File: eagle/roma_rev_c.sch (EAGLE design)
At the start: 23 parts, among them IC1 78L12, U1 LTC3426

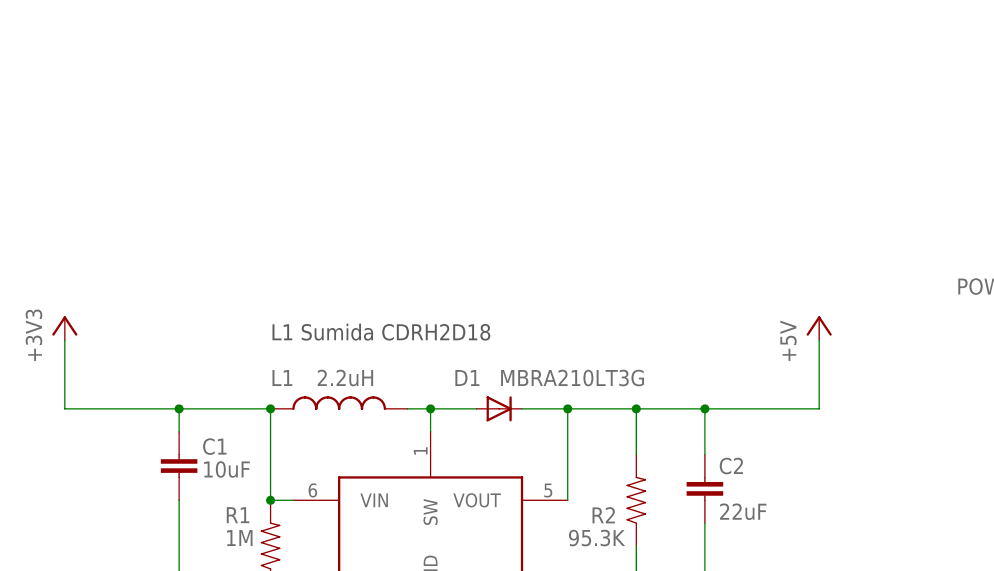
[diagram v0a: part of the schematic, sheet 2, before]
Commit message: Added solder short to get +5V from Odessa 5V without converter.
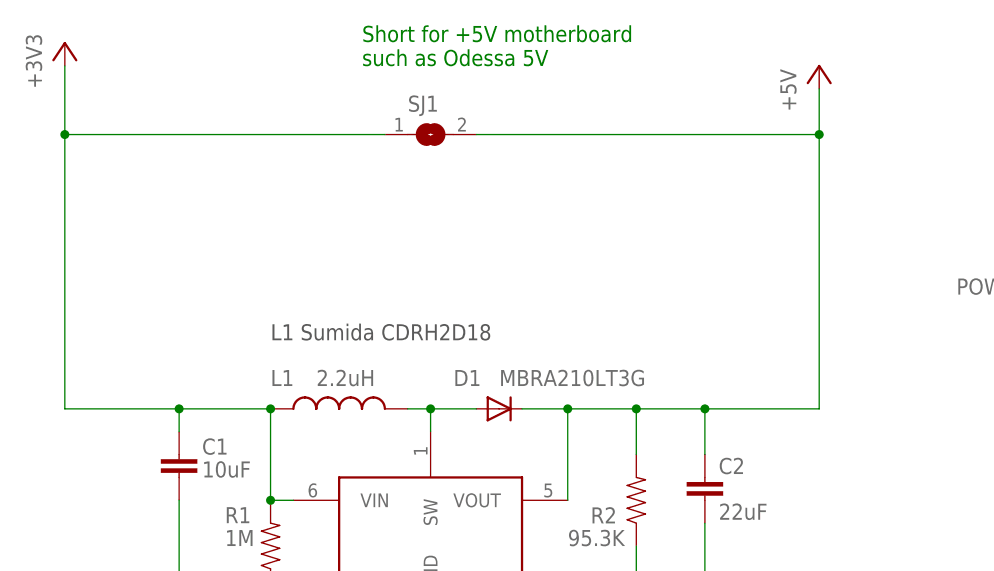
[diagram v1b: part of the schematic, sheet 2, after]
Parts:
- added SJ1: (no value), jumper:SJ
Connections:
- net +3V3: now also SJ1.1
- net +5V: now also SJ1.2
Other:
- note added: "Short for +5V motherboard such as Odessa 5V"
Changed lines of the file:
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@@
 <part name="JP8" library="pinhead" deviceset="PINHD-1X3" device=""/>
 <part name="GND7" library="supply1" deviceset="GND" device=""/>
+<part name="SJ1" library="jumper" deviceset="SJ" device=""/>
 </parts>
 <sheets>
@@
 <text x="220.98" y="129.54" size="1.778" layer="91">1-2  Through 12V regulator
 2-3  Direct to Vin</text>
+<text x="119.38" y="154.94" size="1.778" layer="91">Short for +5V motherboard
+such as Odessa 5V</text>
 </plain>
 <instances>
@@
 </instance>
 <instance part="GND5" gate="1" x="127" y="76.2"/>
-<instance part="+3V1" gate="G$1" x="86.36" y="127"/>
-<instance part="P+1" gate="1" x="170.18" y="127"/>
+<instance part="+3V1" gate="G$1" x="86.36" y="157.48"/>
+<instance part="P+1" gate="1" x="170.18" y="154.94"/>
 <instance part="IC1" gate="1" x="218.44" y="71.12"/>
 <instance part="C4" gate="G$1" x="233.68" y="60.96"/>
@@
 <instance part="JP7" gate="A" x="248.92" y="114.3"/>
 <instance part="VIN1" gate="1" x="193.04" y="86.36"/>
+<instance part="SJ1" gate="1" x="127" y="147.32"/>
 </instances>
 <busses>
@@
 <wire x1="99.06" y1="114.3" x2="99.06" y2="116.84" width="0.1524" layer="91"/>
 <wire x1="99.06" y1="116.84" x2="86.36" y2="116.84" width="0.1524" layer="91"/>
-<wire x1="86.36" y1="116.84" x2="86.36" y2="124.46" width="0.1524" layer="91"/>
+<wire x1="86.36" y1="116.84" x2="86.36" y2="147.32" width="0.1524" layer="91"/>
 <junction x="109.22" y="106.68"/>
 <junction x="109.22" y="116.84"/>
@@
 <pinref part="C1" gate="G$1" pin="1"/>
 <pinref part="+3V1" gate="G$1" pin="+3V3"/>
+<pinref part="SJ1" gate="1" pin="1"/>
+<wire x1="86.36" y1="147.32" x2="86.36" y2="154.94" width="0.1524" layer="91"/>
+<wire x1="121.92" y1="147.32" x2="86.36" y2="147.32" width="0.1524" layer="91"/>
+<junction x="86.36" y="147.32"/>
 </segment>
 </net>
@@
 <wire x1="157.48" y1="116.84" x2="149.86" y2="116.84" width="0.1524" layer="91"/>
 <wire x1="157.48" y1="116.84" x2="170.18" y2="116.84" width="0.1524" layer="91"/>
-<wire x1="170.18" y1="116.84" x2="170.18" y2="124.46" width="0.1524" layer="91"/>
+<wire x1="170.18" y1="116.84" x2="170.18" y2="147.32" width="0.1524" layer="91"/>
 <junction x="142.24" y="116.84"/>
 <junction x="149.86" y="116.84"/>
@@
 <pinref part="C2" gate="G$1" pin="1"/>
 <pinref part="P+1" gate="1" pin="+5V"/>
-</segment>
-</net>
+<pinref part="SJ1" gate="1" pin="2"/>
+<wire x1="170.18" y1="147.32" x2="170.18" y2="152.4" width="0.1524" layer="91"/>
+<wire x1="132.08" y1="147.32" x2="170.18" y2="147.32" width="0.1524" layer="91"/>
+<junction x="170.18" y="147.32"/>
+</segment>
+</net>

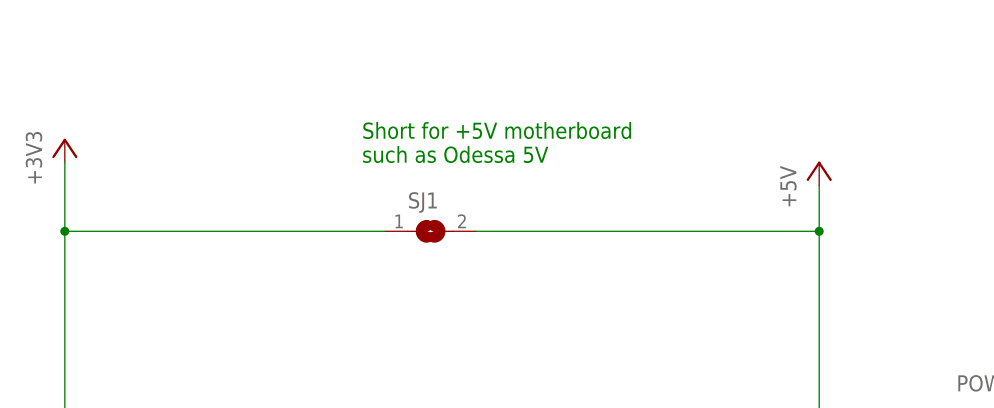
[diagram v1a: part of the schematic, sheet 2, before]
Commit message: Redrawn signal that goes over transceiver protected zone
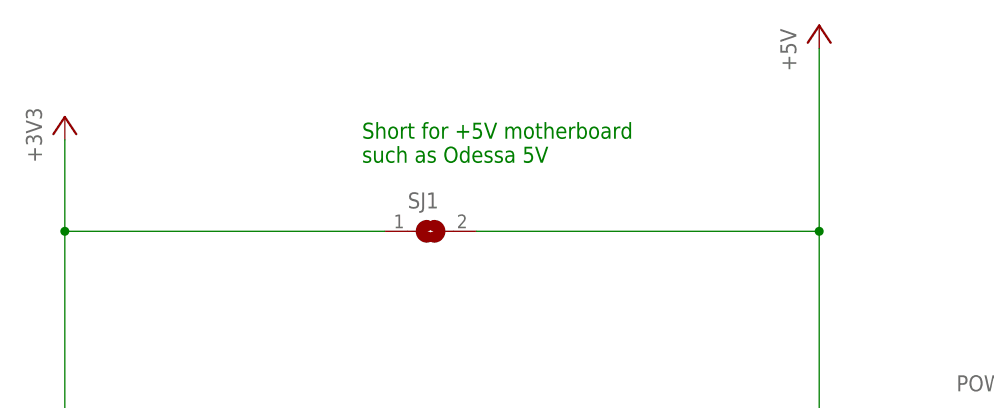
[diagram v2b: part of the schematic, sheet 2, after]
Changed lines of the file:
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@@
 </instance>
 <instance part="GND5" gate="1" x="127" y="76.2"/>
-<instance part="+3V1" gate="G$1" x="86.36" y="157.48"/>
-<instance part="P+1" gate="1" x="170.18" y="154.94"/>
+<instance part="+3V1" gate="G$1" x="86.36" y="160.02"/>
+<instance part="P+1" gate="1" x="170.18" y="170.18"/>
 <instance part="IC1" gate="1" x="218.44" y="71.12"/>
 <instance part="C4" gate="G$1" x="233.68" y="60.96"/>
@@
 <pinref part="+3V1" gate="G$1" pin="+3V3"/>
 <pinref part="SJ1" gate="1" pin="1"/>
-<wire x1="86.36" y1="147.32" x2="86.36" y2="154.94" width="0.1524" layer="91"/>
+<wire x1="86.36" y1="147.32" x2="86.36" y2="157.48" width="0.1524" layer="91"/>
 <wire x1="121.92" y1="147.32" x2="86.36" y2="147.32" width="0.1524" layer="91"/>
 <junction x="86.36" y="147.32"/>
@@
 <pinref part="P+1" gate="1" pin="+5V"/>
 <pinref part="SJ1" gate="1" pin="2"/>
-<wire x1="170.18" y1="147.32" x2="170.18" y2="152.4" width="0.1524" layer="91"/>
+<wire x1="170.18" y1="147.32" x2="170.18" y2="167.64" width="0.1524" layer="91"/>
 <wire x1="132.08" y1="147.32" x2="170.18" y2="147.32" width="0.1524" layer="91"/>
 <junction x="170.18" y="147.32"/>
